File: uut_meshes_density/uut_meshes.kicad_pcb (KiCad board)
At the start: 4 copper layers, 100 x 100 mm, 9 parts, among them J1 Conn_02x10_Counter_Clockwise, J2 Conn_02x10_Counter_Clockwise, J3 Conn_02x10_Counter_Clockwise, J4 Conn_02x10_Counter_Clockwise, J5 MeshAnchor_2W_T0.200mm_S0.200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, J6 MeshAnchor_2W_T0.150mm_S0.150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, J7 MeshAnchor_2W_T0.300mm_S0.300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, J8 MeshAnchor_2W_T0.500mm_S0.500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

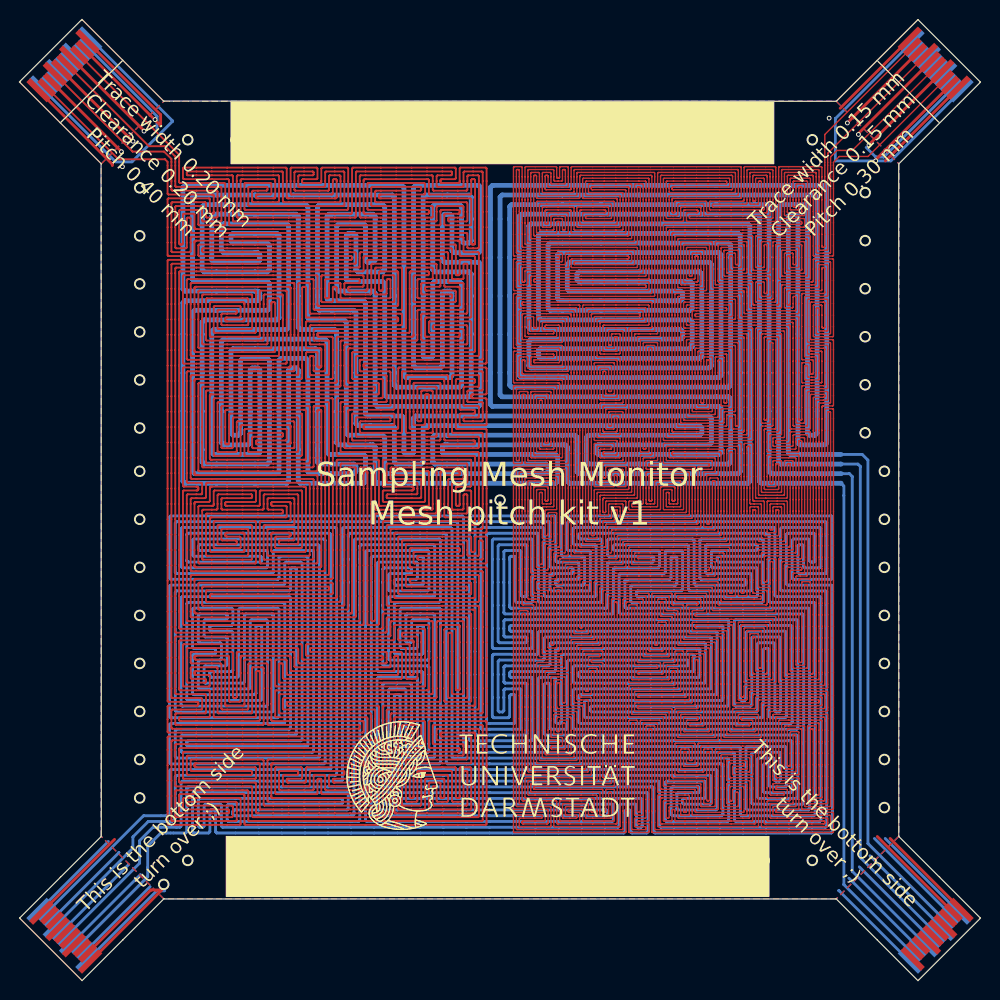
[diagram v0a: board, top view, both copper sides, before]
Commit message: Add mesh length calculation and visualization tool
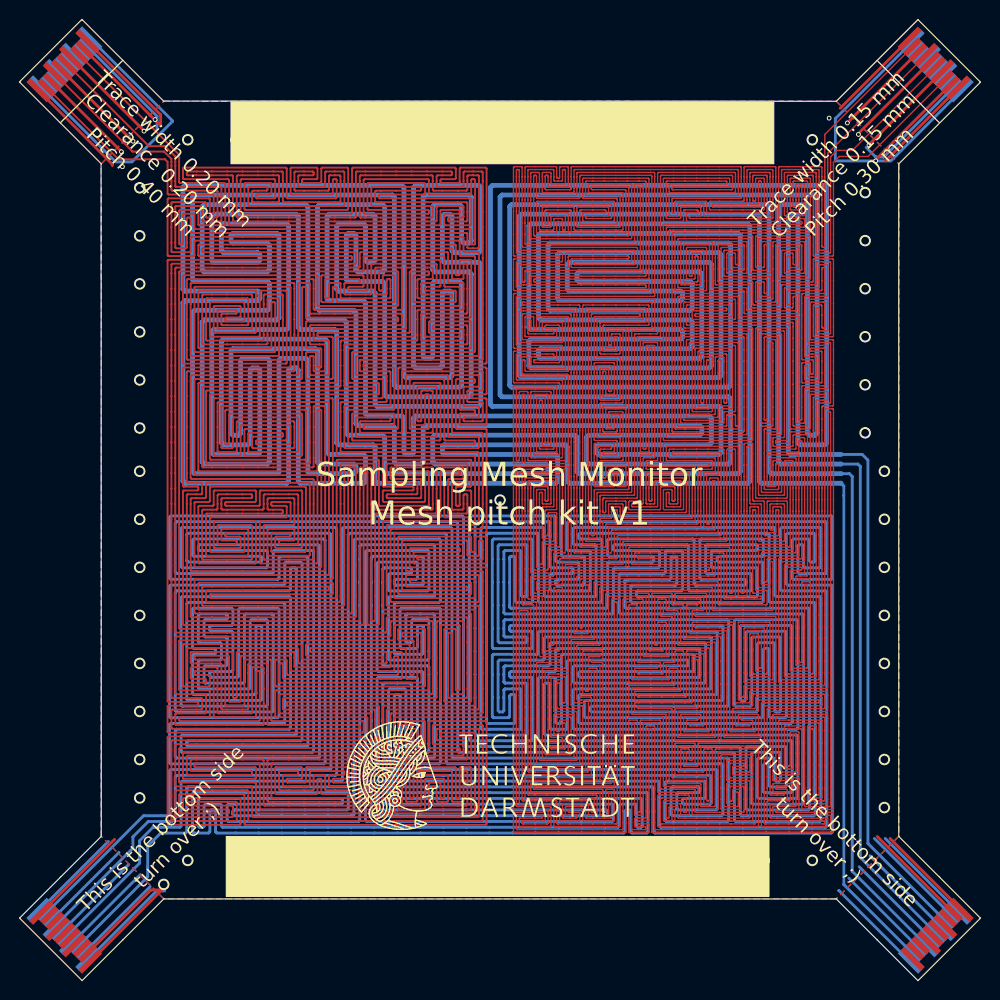
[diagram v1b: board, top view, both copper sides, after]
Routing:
- added copper zone on User.1, net GND
- added copper zone on User.2, net GND
- added copper zone on User.3, net GND
- added copper zone on User.4, net GND
- added copper zone on User.5, net GND
- added copper zone on User.6, net GND
- added copper zone on User.7, net GND
- added copper zone on User.8, net GND
- added copper zone on User.9, net GND
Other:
- copper layers 4 -> 13

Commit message: Add new mesh coupons
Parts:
- removed logo_tu_darmstadt_30.0mm: G*****, logo_tu_darmstadt:logo_tu_darmstadt_30.0mm
- added logo_tu_darmstadt_15.0mm: G*****, logo_tu_darmstadt:logo_tu_darmstadt_15.0mm, F.Cu at (118.2, 135.4)
- added logo_tu_darmstadt_15.0mm: G*****, logo_tu_darmstadt:logo_tu_darmstadt_15.0mm, B.Cu at (183.5, 135.4)
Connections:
- J1 pad 9: GND -> unconnected-(J1-Pin_9-Pad9)
- J3 pad 13: unconnected-(J3-Pin_13-Pad13) -> Net-(J3-Pin_13)
- J3 pad 15: unconnected-(J3-Pin_15-Pad15) -> Net-(J3-Pin_15)
- J3 pad 17: unconnected-(J3-Pin_17-Pad17) -> Net-(J3-Pin_17)
- J3 pad 19: unconnected-(J3-Pin_19-Pad19) -> Net-(J3-Pin_19)
- J3 pad 9: GND -> unconnected-(J3-Pin_9-Pad9)
- J4 pad 9: GND -> unconnected-(J4-Pin_9-Pad9)
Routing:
- net (no net): track 0.00 -> 19452.7 mm
- net mesh0: track 13591.9 -> 0.00 mm
- net mesh1: track 5860.9 -> 0.00 mm
- net GND: track 393.3 -> 358.7 mm, vias 68 -> 73
- net unconnected-(J3-Pin_17-Pad17): track 16.2 -> 0.00 mm
- net Net-(J3-Pin_17): track 0.00 -> 16.2 mm
- net unconnected-(J3-Pin_19-Pad19): track 16.1 -> 0.00 mm
- net Net-(J3-Pin_19): track 0.00 -> 16.1 mm
- net unconnected-(J3-Pin_15-Pad15): track 15.8 -> 0.00 mm
- net Net-(J3-Pin_15): track 0.00 -> 15.8 mm
- net unconnected-(J3-Pin_13-Pad13): track 15.2 -> 0.00 mm
- net Net-(J3-Pin_13): track 0.00 -> 15.2 mm
- removed copper zone on User.1, net GND
- removed copper zone on User.2, net GND
- removed copper zone on User.3, net GND
- removed copper zone on User.4, net GND
- removed copper zone on User.5, net GND
- removed copper zone on User.6, net GND
- removed copper zone on User.7, net GND
- removed copper zone on User.8, net GND
- removed copper zone on User.9, net GND
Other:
- outline, holes or cut-outs redrawn
- copper layers 13 -> 4
- board text added: "(bottom)"
- board text added: "1"
- board text added: "10"
- board text added: "11"
- board text added: "12"
- board text added: "13"
- board text added: "14"
- board text added: "2"
- board text added: "3"
- board text added: "4"
- board text added: "5"
- board text added: "6"
- board text added: "7"
- board text added: "8"
- board text added: "9"
- board text added: "A"
- board text added: "B"
- board text added: "C"
- board text added: "D"
- board text added: "E"
- board text added: "F"
- board text added: "G"
- board text added: "H"
- board text added: "I"
- board text added: "J"
- board text added: "K"
- board text added: "L"
- board text added: "M"
- board text added: "N"
- board text added: "Sampling Mesh Monitor Mesh pitch kit v2"
- board text added: "Serial"
- board text added: "pitch 0.3mm"
- board text added: "pitch 0.4mm"
- board text added: "pitch 0.60mm"
- board text added: "pitch 1.00mm"
- board text removed: "Sampling Mesh Monitor Mesh pitch kit v1"
- board text removed: "This is the bottom side turn over ;)"
- board text removed: "Trace width 0.15 mm Clearance 0.15 mm Pitch 0.30 mm"
- board text removed: "Trace width 0.20 mm Clearance 0.20 mm Pitch 0.40 mm"
- board text removed: "Trace width 0.30 mm Clearance 0.30 mm Pitch 0.60 mm"
- board text removed: "Trace width 0.50 mm Clearance 0.50 mm Pitch 1.00 mm"
